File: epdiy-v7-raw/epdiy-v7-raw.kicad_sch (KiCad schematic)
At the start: 111 parts, among them CN1 WP27D-S050VA3-R15000, IC1 MPU-6500, J1 USB_C_Receptacle_USB2.0, J2 EXTENSION_HEADER, J3 SIGNALS_HEADER, J4 XF2M-3315-1A, J5 S2B-PH-SM4-TB_LF__SN_, J6 THD2528-11SD-GF, Q1 AO3401A, SW1 TC-0522C-1.7-160G, SW3 K2-1806SQ-A2DW-04, SW4 K2-1806SQ-A2DW-04, SW5 K2-1806SQ-A2DW-04, U1 RT9080-33GJ5, U10 ED060XC5, U11 TP4056, U3 TPS651851RSLR, U4 USBLC6-2P6, U8 ESP32-S3-WROOM-1, Y1 RV-3032-C7

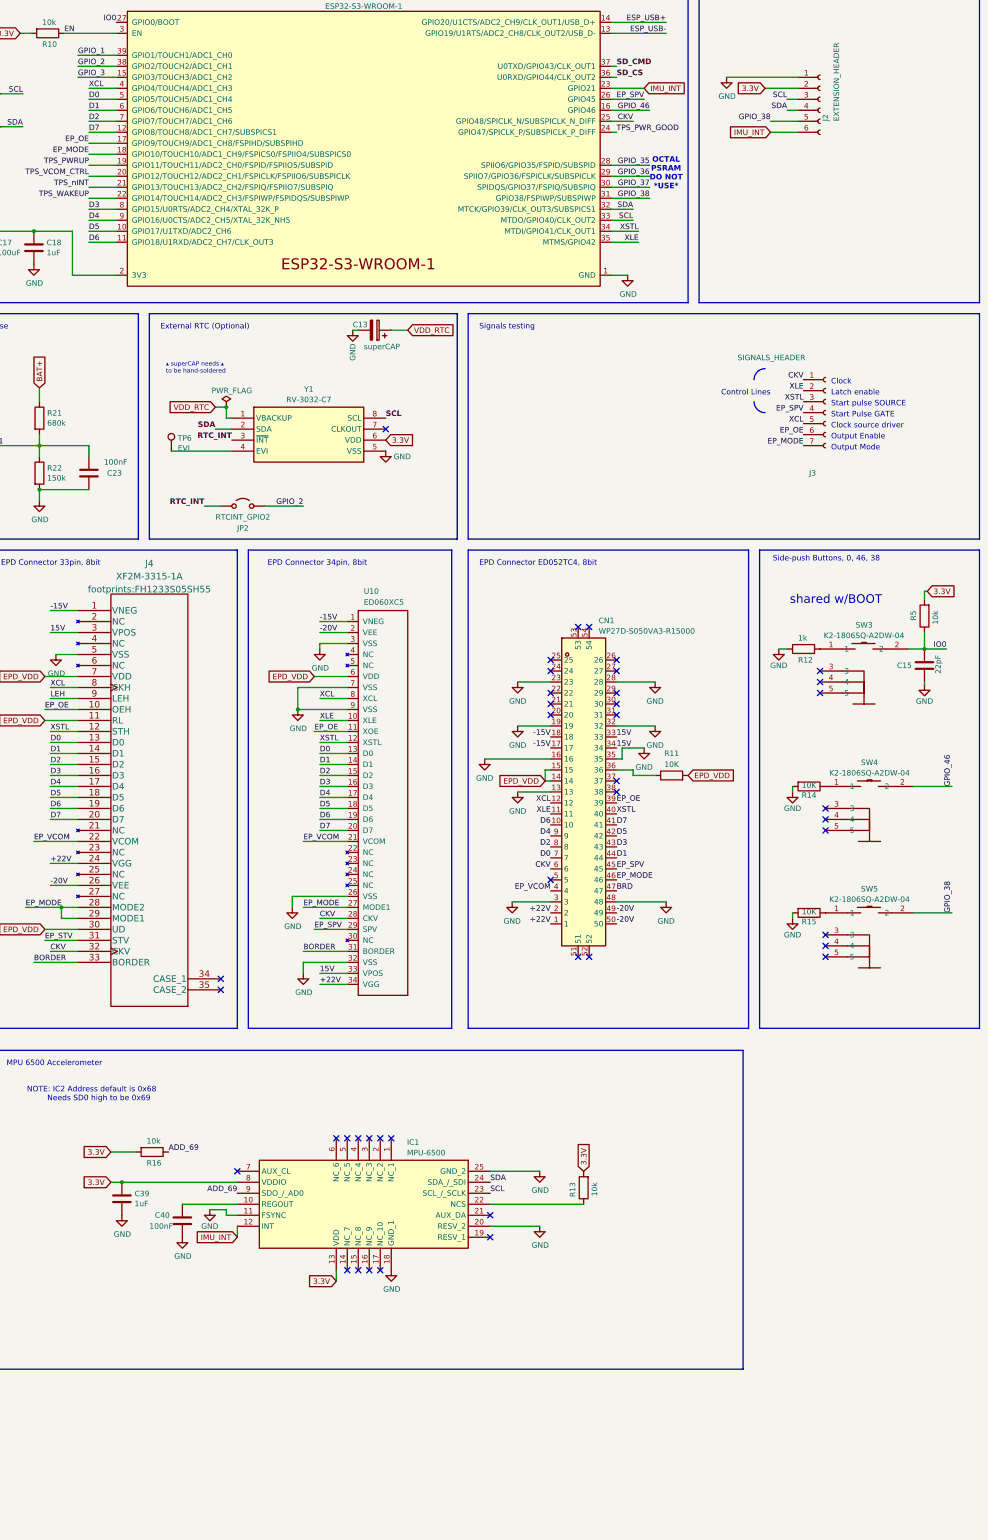
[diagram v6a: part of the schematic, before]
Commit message: Add single buffer to XCL to decouple when EPD_VDD is low
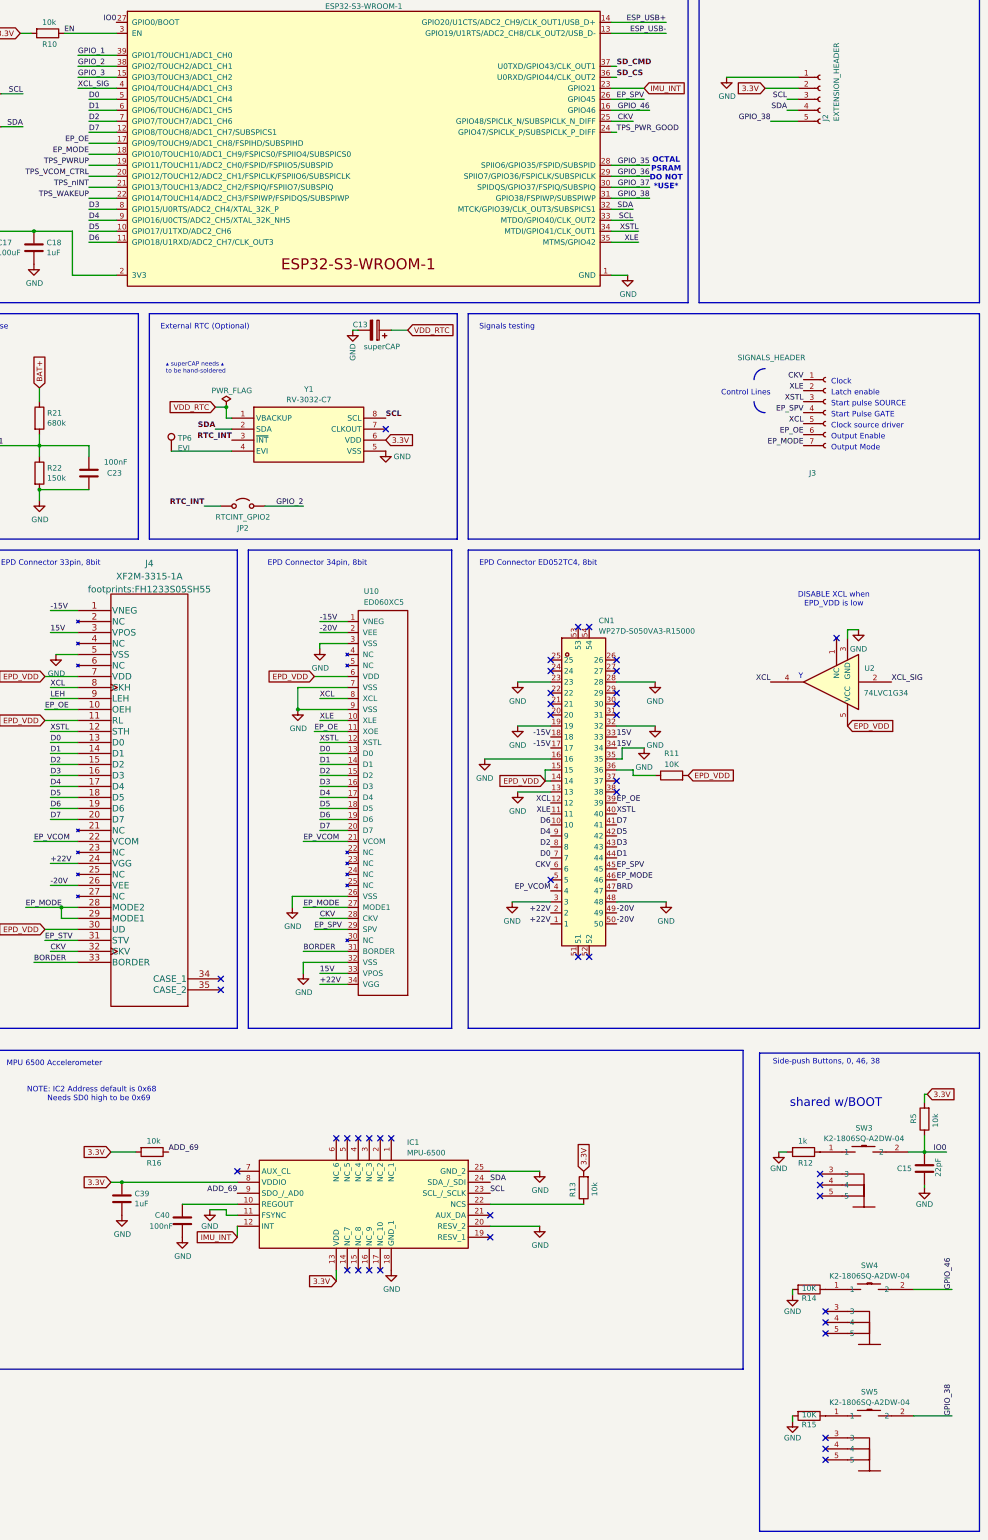
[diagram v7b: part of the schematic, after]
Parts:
- removed J2: EXTENSION_HEADER, Connector_PinHeader_2.54mm:PinHeader_1x06_P2.54mm_Vertical, symbol Connector:Conn_01x06_Socket
- added J2: EXTENSION_HEADER, Connector_PinHeader_2.54mm:PinHeader_1x05_P2.54mm_Vertical, symbol Connector:Conn_01x05_Socket
- added U2: 74LVC1G34, Package_TO_SOT_SMD:SOT-23-5, symbol 74xGxx:74LVC1G34
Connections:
- net 3.3V: now also J2.2 (Pin_2)
- net EPD_VDD: now also U2.5 (VCC)
- net GND: now also J2.1 (Pin_1), U2.3 (GND)
- net GPIO_38: now also J2.5 (Pin_5)
- net SCL: now also J2.3 (Pin_3)
- net SDA: now also J2.4 (Pin_4)
- net XCL: now also U2.4; no longer U8.4 (GPIO4/TOUCH4/ADC1_CH3)
- new net XCL_SIG: U2.2, U8.4 (GPIO4/TOUCH4/ADC1_CH3)
- no-connect marks 60 -> 61
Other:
- note added: "DISABLE XCL when EPD_VDD is low"
- note added: "Y"
- moved on the sheet: C15, R12, R14, R15, R5, SW3, SW4, SW5
